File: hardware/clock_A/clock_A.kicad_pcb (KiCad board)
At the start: 2 copper layers, 119 x 92 mm, 225 parts, among them J1 RJ45, J10 KH-BNC50-3511, J11 KH-BNC50-3511, J12 Conn_01x08_Pin, J13 KH-BNC50-3511, J14 Conn_01x02_Pin, J2 Conn_01x03, J3 KH-BNC50-3511, J4 USB_C_Receptacle, J5 Conn_01x06_Pin, J6 Conn_01x03_Pin, J7 KH-BNC50-3511, J8 Conn_01x02_Pin, J9 KH-BNC50-3511, Q1 2N7002, Q10 2N7002, Q9 2N7002, SW1 SW_Push_4PDT, SW2 SW_SPDT, U1 ADA4807-1, U10 STM32F405RGTx, U11 AMS1117-3.3, U12 BA50DD0WHFP-TR, U13 M24C02-RMN, U14 CH340C, U15 USBLC6-2P6, U16 TLV3603DCKR, U17 SN74LVC1G14DBV, U18 TMP112AIDRLR, U19 SN74LVC1G14DBV, U2 SN74LVC1G14DBV, U20 SN74LVC1G14DBV, U21 SN74LVC1G14DBV, U23 TPS63060, U3 SN74LVC1G14DBV, U4 ADA4807-1, U5 ADA4807-1, U6 TLV3603DCKR, U7 SN74LVC1G14DBV, U8 TLV3603DCKR, U9 L78L05_SOT89, Y1 MultiOsc, Y2 16MHz

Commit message: updade clock order with correct diode. Fixes #339
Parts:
- D4: value SDM20U30-7 -> B5819W SL
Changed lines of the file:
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@@
 			)
 		)
-		(property "Value" "SDM20U30-7"
+		(property "Value" "B5819W SL"
 			(at 0 2.1 -90)
 			(layer "F.Fab")
@@
 			)
 		)
-		(property "Datasheet" "https://www.vishay.com/docs/85748/1n4148w.pdf"
+		(property "Datasheet" ""
 			(at 0 0 -90)
 			(unlocked yes)
@@
 			)
 		)
-		(property "Description" "75V 0.15A Fast Switching Diode, SOD-123"
+		(property "Description" "40V 600mV@1A 1A SOD-123 Schottky Barrier Diodes"
 			(at 0 0 -90)
 			(unlocked yes)
@@
 			)
 		)
-		(property "JLCPCB Part #" "C91235"
+		(property "JLCPCB Part #" "C8598"
 			(at 0 0 0)
 			(layer "F.Fab")

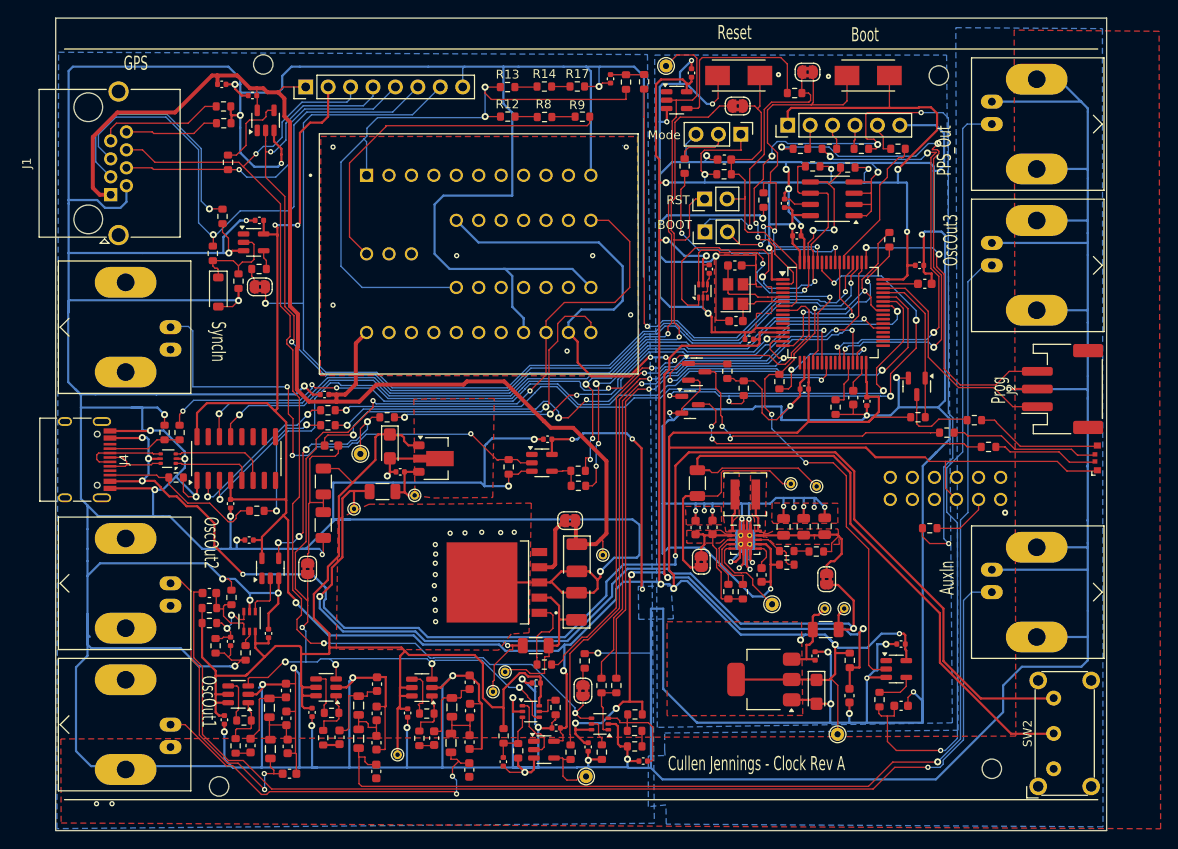
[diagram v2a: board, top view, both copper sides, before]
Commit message: remove tantium caps from clock board
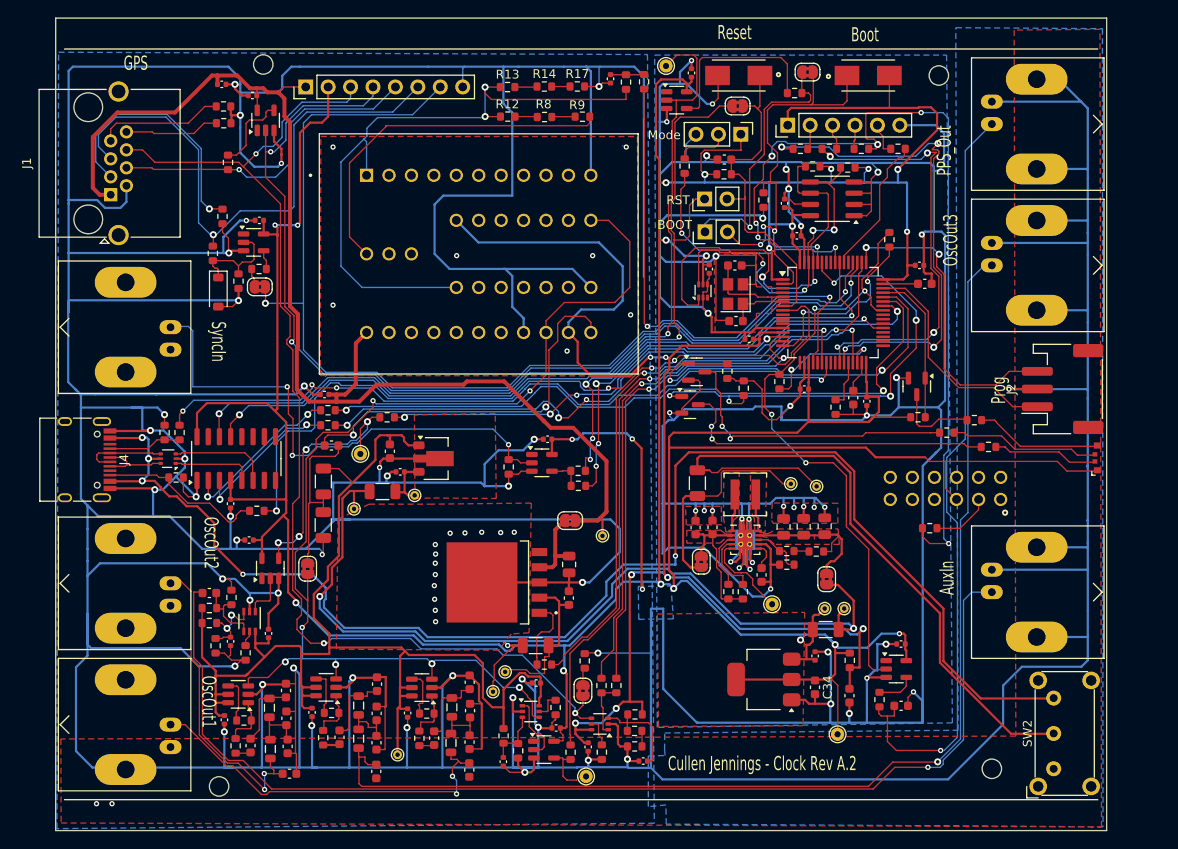
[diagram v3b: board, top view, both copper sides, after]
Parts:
- removed C44: 33u, Capacitor_Tantalum_SMD:CP_EIA-3528-21_Kemet-B
- added C43: 10u, Capacitor_SMD:C_0603_1608Metric, F.Cu at (132.8, 87.0)
- C34: footprint Capacitor_Tantalum_SMD:CP_EIA-3216-18_Kemet-A -> Capacitor_SMD:C_0603_1608Metric
- C41: value 10u -> 22u; footprint Capacitor_Tantalum_SMD:CP_EIA-3216-18_Kemet-A -> Capacitor_SMD:C_0805_2012Metric
- C42: value 33u -> 2u2; footprint Capacitor_Tantalum_SMD:CP_EIA-3528-21_Kemet-B -> Capacitor_SMD:C_0603_1608Metric
- moved C34 55.3 mm to (181.0, 113.8)
- moved C41 31.5 mm to (153.1, 99.9)
- moved C42 4.65 mm to (153.1, 103.7)
- moved TP3 2.19 mm to (156.9, 96.6)
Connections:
- C34 pad 1: +5VA -> +3.3V
- C41 pad 1: +3.3V -> Net-(JP4-A)
- C42 pad 1: +5V -> GND
- C42 pad 2: GND -> Net-(U12-VCC)
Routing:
- net GND: track 1590.3 -> 1582.6 mm, vias 98 -> 99
- net +5V: track 141.8 -> 137.0 mm
- net Net-(J10-In): track 89.3 -> 87.6 mm
- net Net-(JP4-A): track 7.31 -> 8.92 mm
- net Net-(J9-In): track 57.1 -> 58.5 mm
- net +5VA: track 138.8 -> 139.9 mm
- net Net-(U12-VCC): track 18.1 -> 17.6 mm
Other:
- board text added: "Cullen Jennings - Clock Rev A.2"
- board text removed: "Cullen Jennings - Clock Rev A"

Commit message: generating Clock Rev A.2
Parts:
- TP1, TP10, TP4, TP7, TP8: footprint TestPoint:TestPoint_THTPad_D1.5mm_Drill0.7mm -> TestPoint:TestPoint_THTPad_D1.0mm_Drill0.5mm
- U16: footprint blinky_footprints:SC70_DCK_TEX -> Package_TO_SOT_SMD:SOT-363_SC-70-6
- moved C52 0.47 mm to (119.6, 107.7)
- moved U16 0.28 mm to (117.2, 106.3)
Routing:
- net +3.3V: track 549.3 -> 549.9 mm
- net Net-(U16-LE/HYS): track 1.79 -> 2.29 mm
- net GND: track 1582.6 -> 1582.4 mm, vias 99 -> 100

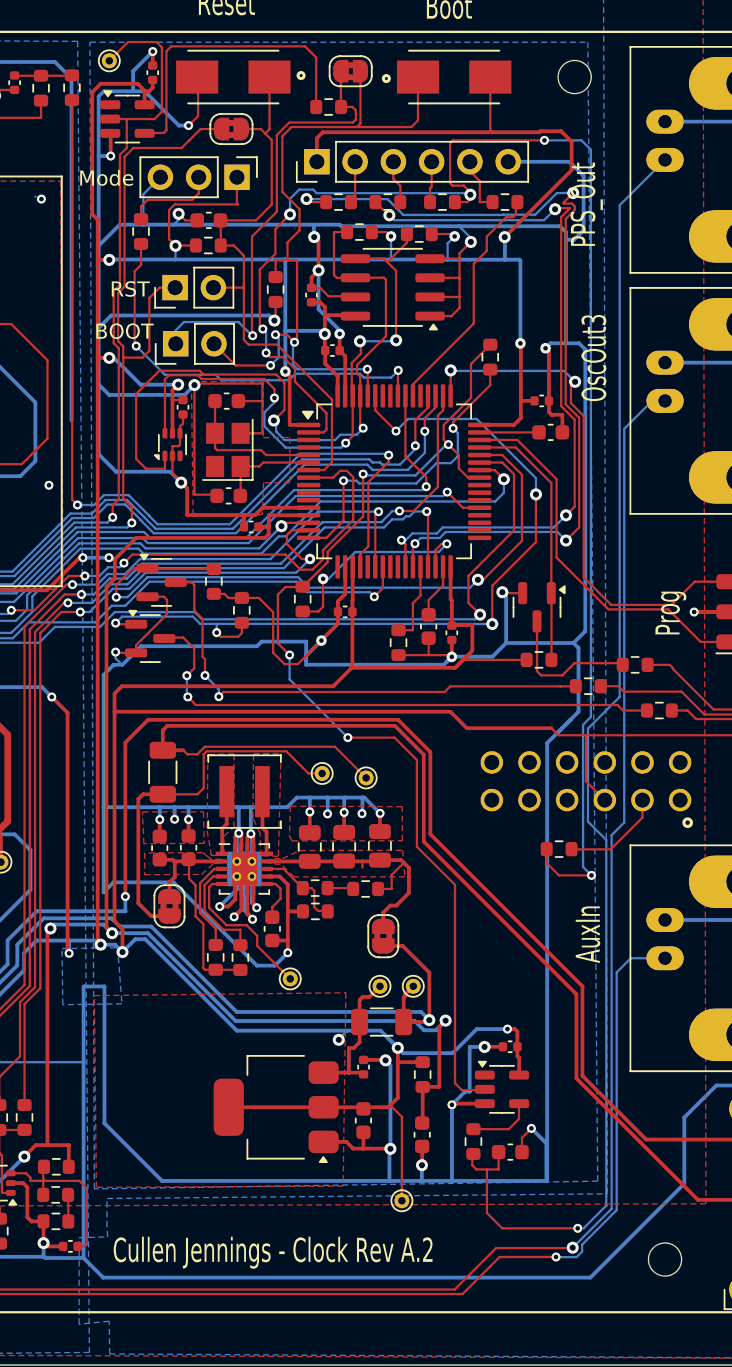
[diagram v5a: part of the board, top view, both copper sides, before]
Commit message: update all harware revs
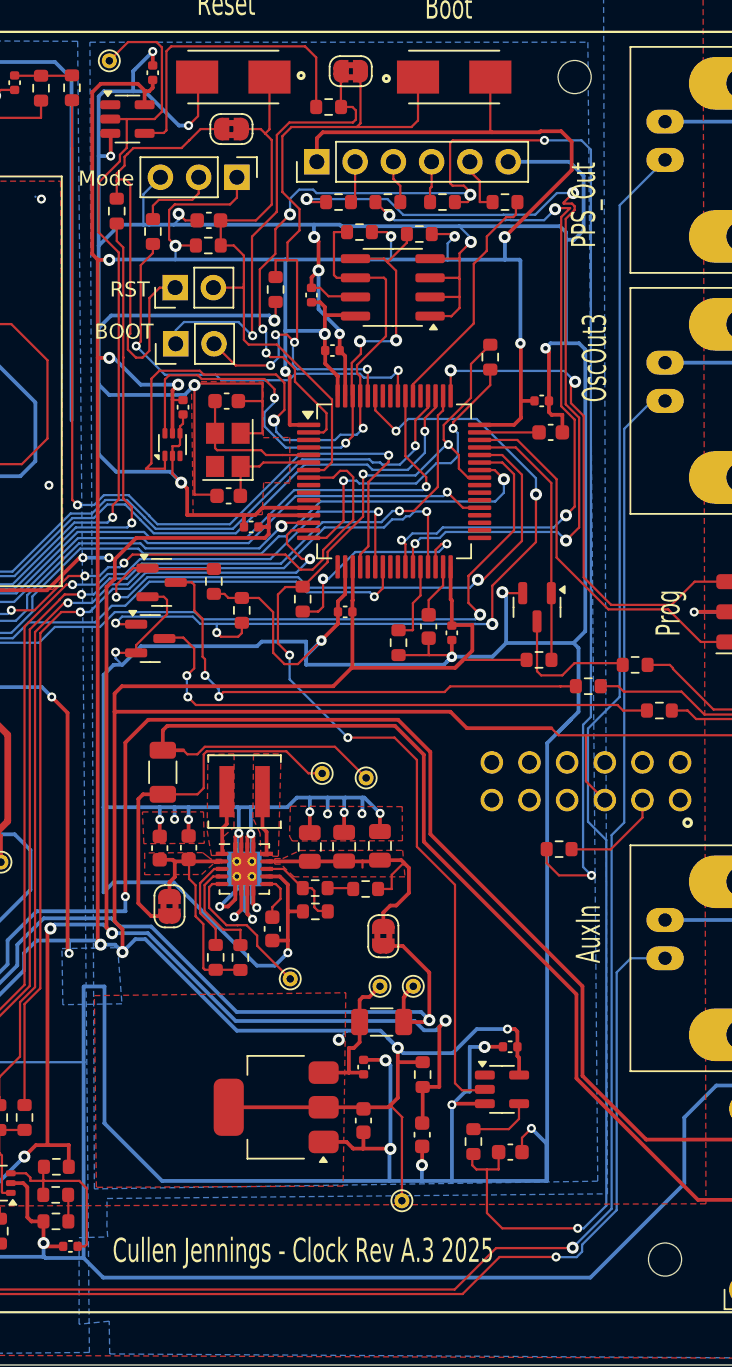
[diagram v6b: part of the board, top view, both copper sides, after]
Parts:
- added R40: 1K0, Resistor_SMD:R_0603_1608Metric, F.Cu at (164.6, 53.4)
- FB1: value 120Ω@100MHz -> 120Ω@100MHz
- Y2: value 16MHz -> 16MHz
- moved R80 0.79 mm to (167.0, 54.8)
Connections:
- J8 pad 1: /USB_DTR -> Net-(J8-Pin_1)
- JP1 pad 1: /USB_DTR -> Net-(J8-Pin_1)
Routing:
- net Net-(J8-Pin_1): track 0.00 -> 29.7 mm
- net /USB_DTR: track 97.3 -> 78.1 mm
- net /USB_RTS: track 97.8 -> 98.6 mm
- net Net-(J6-Pin_2): track 6.10 -> 5.34 mm
- net /SCL: track 46.2 -> 45.6 mm
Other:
- board text added: "Cullen Jennings - Clock Rev A.3 2025"
- board text removed: "Cullen Jennings - Clock Rev A.2"
